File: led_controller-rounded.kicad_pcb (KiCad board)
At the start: 2 copper layers, 88.9 x 46.2 mm, 83 parts, among them J1 Screw_Terminal_01x02, J10 Conn_01x03, J2 SJ-3524-SMT, J3 Conn_01x03, J4 Conn_01x03, J5 Conn_01x03, J6 Conn_01x03, J7 Conn_01x03, J8 Conn_01x03, J9 Conn_01x03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

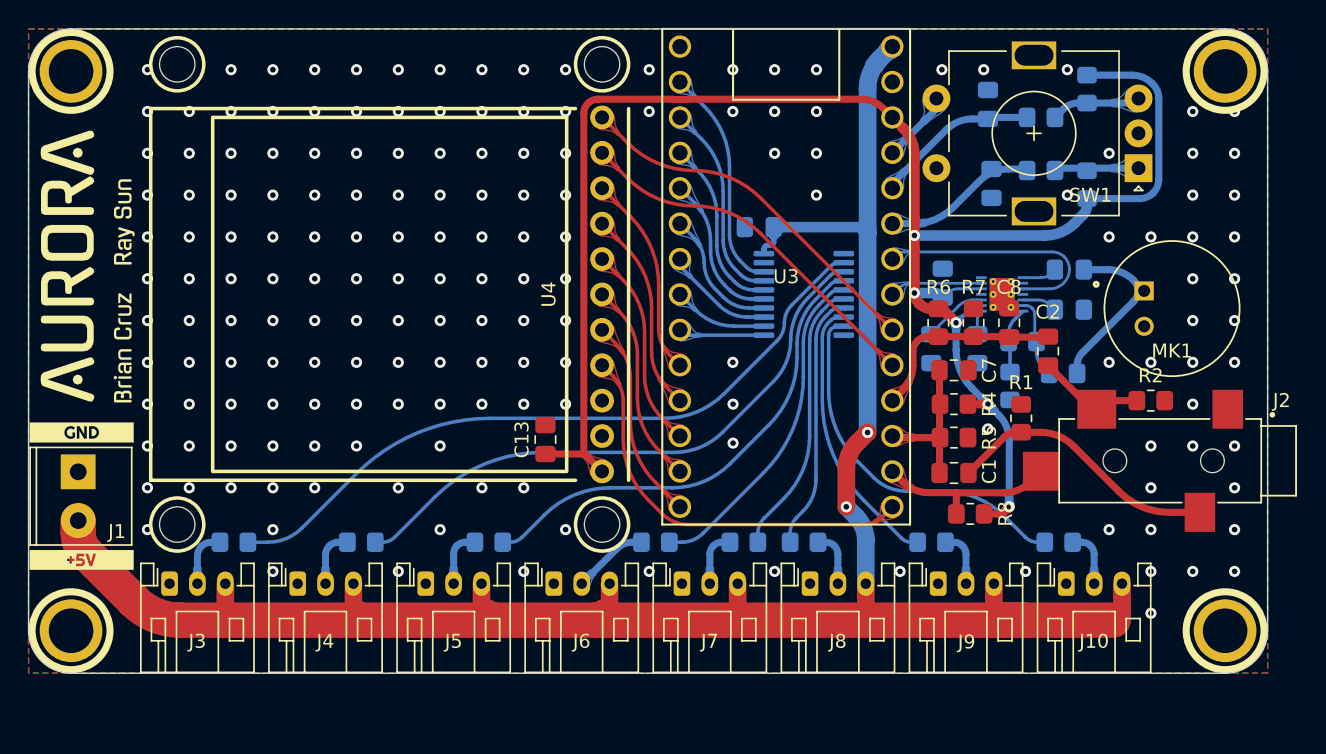
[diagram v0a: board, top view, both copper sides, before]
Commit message: Switch to molex nano-fit connectors
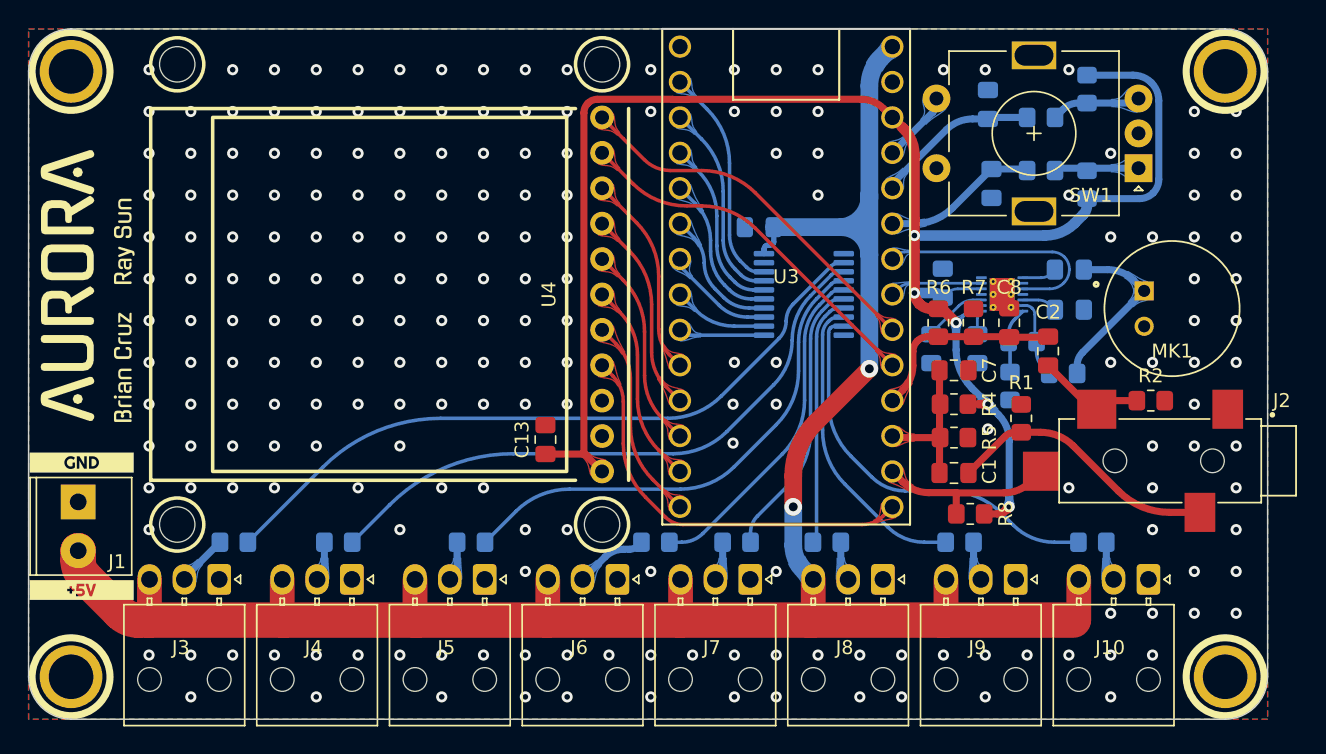
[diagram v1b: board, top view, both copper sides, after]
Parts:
- removed kibuzzard-62AD6AEC, kibuzzard-62AD6AEC1, kibuzzard-62AD6AEC2, kibuzzard-62AD6AEC3, kibuzzard-62AD6AEC4, kibuzzard-62AD6AEC5, kibuzzard-62AD6AEC6, kibuzzard-62AD6AEC7: G***, kibuzzard-62AD6AEC
- removed kibuzzard-62AD6B04, kibuzzard-62AD6B1, kibuzzard-62AD6B2, kibuzzard-62AD6B3, kibuzzard-62AD6B4, kibuzzard-62AD6B5, kibuzzard-62AD6B6, kibuzzard-62AD6B7: G***, kibuzzard-62AD6B04
- removed kibuzzard-62AD6B13: G***, kibuzzard-62AD6B13
- removed kibuzzard-62AD6BA8: G***, kibuzzard-62AD6BA8
- removed kibuzzard-62AD6BC2: G***, kibuzzard-62AD6BC2
- removed kibuzzard-62AD6C16: G***, kibuzzard-62AD6C16
- removed kibuzzard-62AD6C27: G***, kibuzzard-62AD6C27
- removed kibuzzard-62AD6C38: G***, kibuzzard-62AD6C38
- removed kibuzzard-62AD6C4C: G***, kibuzzard-62AD6C4C
- removed kibuzzard-62AD6C62: G***, kibuzzard-62AD6C62
- J10, J3, J4, J5, J6, J7, J8, J9: footprint Connector_JST:JST_PH_S3B-PH-K_1x03_P2.00mm_Horizontal -> Connector_Molex:Molex_Nano-Fit_105313-xx03_1x03_P2.50mm_Horizontal
- moved J10 5.90 mm to (170.5, 126.6), turned to -90 degrees
- moved J9 5.57 mm to (161.0, 126.6), turned to -90 degrees
- moved J8 5.24 mm to (151.5, 126.6), turned to -90 degrees
- moved J7 4.91 mm to (141.9, 126.6), turned to -90 degrees
- moved J6 4.57 mm to (132.4, 126.6), turned to -90 degrees
- moved J5 4.24 mm to (122.9, 126.6), turned to -90 degrees
- moved J4 3.91 mm to (113.4, 126.6), turned to -90 degrees
- moved J3 3.57 mm to (103.8, 126.6), turned to -90 degrees
- moved H3 3.30 mm to (93.2, 133.6)
- moved H4 3.30 mm to (176.0, 133.6)
- moved R20 2.41 mm to (166.5, 124.0)
- moved kibuzzard-62AD66A7 2.16 mm to (94.0, 127.4)
- moved J1 2.16 mm to (93.7, 121.1)
- moved kibuzzard-62AD66B6 2.16 mm to (94.0, 118.2)
- moved R19 2.02 mm to (157.0, 124.0)
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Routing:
- net Net-(R20-Pad2): track 26.3 -> 28.9 mm
- net Net-(R19-Pad2): track 19.9 -> 22.1 mm
- net Net-(R15-Pad2): track 34.3 -> 36.1 mm
- net Net-(R14-Pad2): track 42.4 -> 44.2 mm
- net /LED_OUT_1: track 4.14 -> 2.84 mm
- net /LED_OUT_7: track 4.13 -> 2.84 mm
- net /LED_OUT_2: track 4.13 -> 2.84 mm
- net /LED_OUT_6: track 4.07 -> 2.84 mm
- net /LED_OUT_4: track 4.04 -> 2.84 mm
- net /LED_OUT_5: track 4.02 -> 2.84 mm
- net +5V: track 152.6 -> 153.4 mm
- net Net-(C3-Pad2): track 12.2 -> 12.7 mm
- net GND: vias 175 -> 210
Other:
- board size 88.9 x 46.2 mm -> 88.9 x 49.5 mm

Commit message: Revert "Switch to molex nano-fit connectors"
This reverts commit 9b38a182e228fa806dde65dc415f981188c8a403.
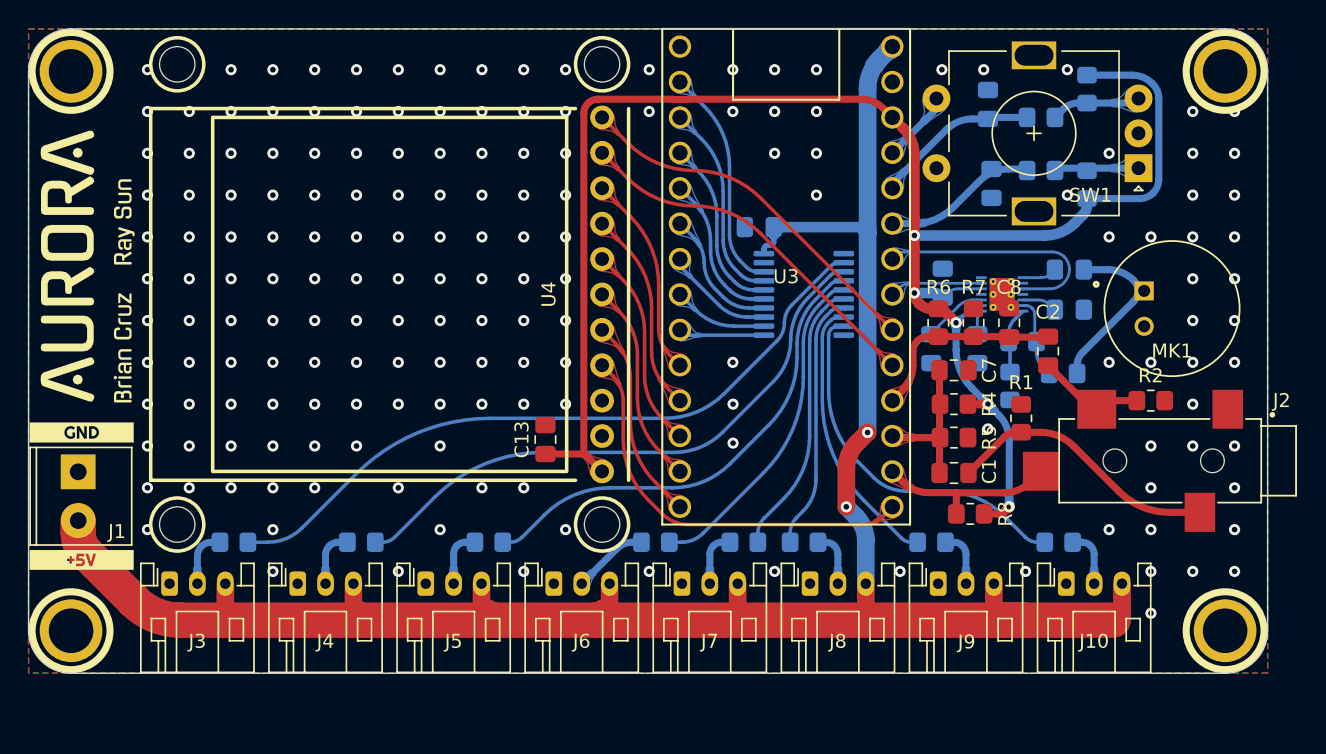
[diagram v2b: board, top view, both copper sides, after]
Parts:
- added kibuzzard-62AD6AEC: G***, kibuzzard-62AD6AEC, B.Cu at (100.3, 131.3)
- added kibuzzard-62AD6AEC1: G***, kibuzzard-62AD6AEC, B.Cu at (109.5, 131.3)
- added kibuzzard-62AD6AEC2: G***, kibuzzard-62AD6AEC, B.Cu at (118.7, 131.3)
- added kibuzzard-62AD6AEC3: G***, kibuzzard-62AD6AEC, B.Cu at (127.9, 131.3)
- added kibuzzard-62AD6AEC4: G***, kibuzzard-62AD6AEC, B.Cu at (137.1, 131.3)
- added kibuzzard-62AD6AEC5: G***, kibuzzard-62AD6AEC, B.Cu at (146.2, 131.3)
- added kibuzzard-62AD6AEC6: G***, kibuzzard-62AD6AEC, B.Cu at (155.4, 131.3)
- added kibuzzard-62AD6AEC7: G***, kibuzzard-62AD6AEC, B.Cu at (164.6, 131.3)
- added kibuzzard-62AD6B04: G***, kibuzzard-62AD6B04, B.Cu at (104.3, 131.3)
- added kibuzzard-62AD6B1: G***, kibuzzard-62AD6B04, B.Cu at (113.5, 131.3)
- added kibuzzard-62AD6B13: G***, kibuzzard-62AD6B13, B.Cu at (102.3, 131.3)
- added kibuzzard-62AD6B2: G***, kibuzzard-62AD6B04, B.Cu at (122.7, 131.3)
- added kibuzzard-62AD6B3: G***, kibuzzard-62AD6B04, B.Cu at (131.9, 131.3)
- added kibuzzard-62AD6B4: G***, kibuzzard-62AD6B04, B.Cu at (141.1, 131.3)
- added kibuzzard-62AD6B5: G***, kibuzzard-62AD6B04, B.Cu at (150.2, 131.3)
- added kibuzzard-62AD6B6: G***, kibuzzard-62AD6B04, B.Cu at (159.4, 131.3)
- added kibuzzard-62AD6B7: G***, kibuzzard-62AD6B04, B.Cu at (168.6, 131.3)
- added kibuzzard-62AD6BA8: G***, kibuzzard-62AD6BA8, B.Cu at (111.5, 131.3)
- added kibuzzard-62AD6BC2: G***, kibuzzard-62AD6BC2, B.Cu at (120.7, 131.3)
- added kibuzzard-62AD6C16: G***, kibuzzard-62AD6C16, B.Cu at (129.9, 131.3)
- added kibuzzard-62AD6C27: G***, kibuzzard-62AD6C27, B.Cu at (139.0, 131.3)
- added kibuzzard-62AD6C38: G***, kibuzzard-62AD6C38, B.Cu at (148.2, 131.3)
- added kibuzzard-62AD6C4C: G***, kibuzzard-62AD6C4C, B.Cu at (157.4, 131.3)
- added kibuzzard-62AD6C62: G***, kibuzzard-62AD6C62, B.Cu at (166.6, 131.3)
- J10, J3, J4, J5, J6, J7, J8, J9: footprint Connector_Molex:Molex_Nano-Fit_105313-xx03_1x03_P2.50mm_Horizontal -> Connector_JST:JST_PH_S3B-PH-K_1x03_P2.00mm_Horizontal
- moved J10 5.90 mm to (164.6, 126.9), turned to 0 degrees
- moved J9 5.57 mm to (155.4, 126.9), turned to 0 degrees
- moved J8 5.24 mm to (146.2, 126.9), turned to 0 degrees
- moved J7 4.91 mm to (137.1, 126.9), turned to 0 degrees
- moved J6 4.57 mm to (127.9, 126.9), turned to 0 degrees
- moved J5 4.24 mm to (118.7, 126.9), turned to 0 degrees
- moved J4 3.91 mm to (109.5, 126.9), turned to 0 degrees
- moved J3 3.57 mm to (100.3, 126.9), turned to 0 degrees
- moved H3 3.30 mm to (93.2, 130.3)
- moved H4 3.30 mm to (176.0, 130.3)
- moved R20 2.41 mm to (164.1, 124.0)
- moved kibuzzard-62AD66A7 2.16 mm to (94.0, 125.2)
- moved J1 2.16 mm to (93.7, 118.9)
- moved kibuzzard-62AD66B6 2.16 mm to (94.0, 116.1)
- moved R19 2.02 mm to (155.0, 124.0)
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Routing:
- net Net-(R20-Pad2): track 28.9 -> 26.3 mm
- net Net-(R19-Pad2): track 22.1 -> 19.9 mm
- net Net-(R15-Pad2): track 36.1 -> 34.3 mm
- net Net-(R14-Pad2): track 44.2 -> 42.4 mm
- net /LED_OUT_1: track 2.84 -> 4.14 mm
- net /LED_OUT_7: track 2.84 -> 4.13 mm
- net /LED_OUT_2: track 2.84 -> 4.13 mm
- net /LED_OUT_6: track 2.84 -> 4.07 mm
- net /LED_OUT_4: track 2.84 -> 4.04 mm
- net /LED_OUT_5: track 2.84 -> 4.02 mm
- net +5V: track 153.4 -> 152.6 mm
- net Net-(C3-Pad2): track 12.7 -> 12.2 mm
- net GND: vias 210 -> 175
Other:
- board size 88.9 x 49.5 mm -> 88.9 x 46.2 mm

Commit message: verified by Brian, create gerbers
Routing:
- net Net-(C3-Pad2): track 12.2 -> 12.7 mm
